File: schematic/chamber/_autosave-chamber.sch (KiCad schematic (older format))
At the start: 13 parts

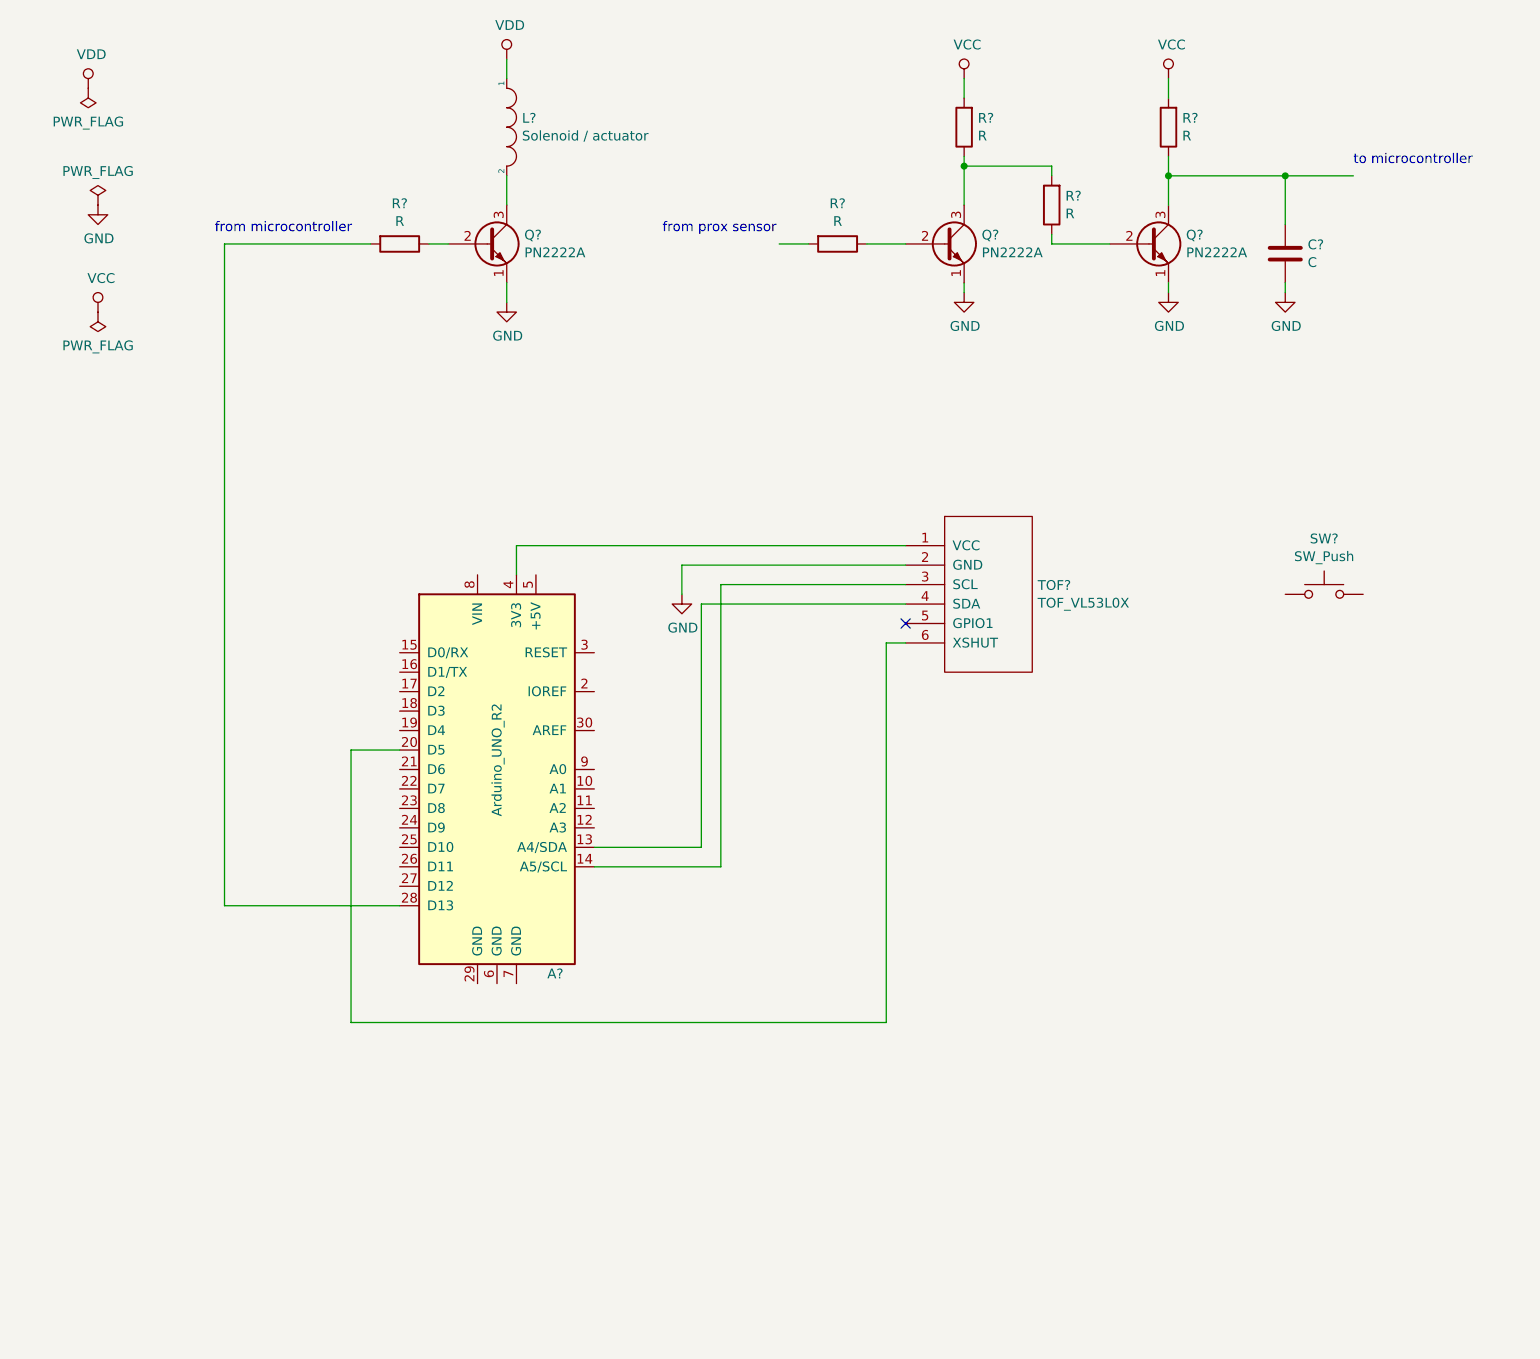
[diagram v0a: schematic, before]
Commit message: remove unused declarations
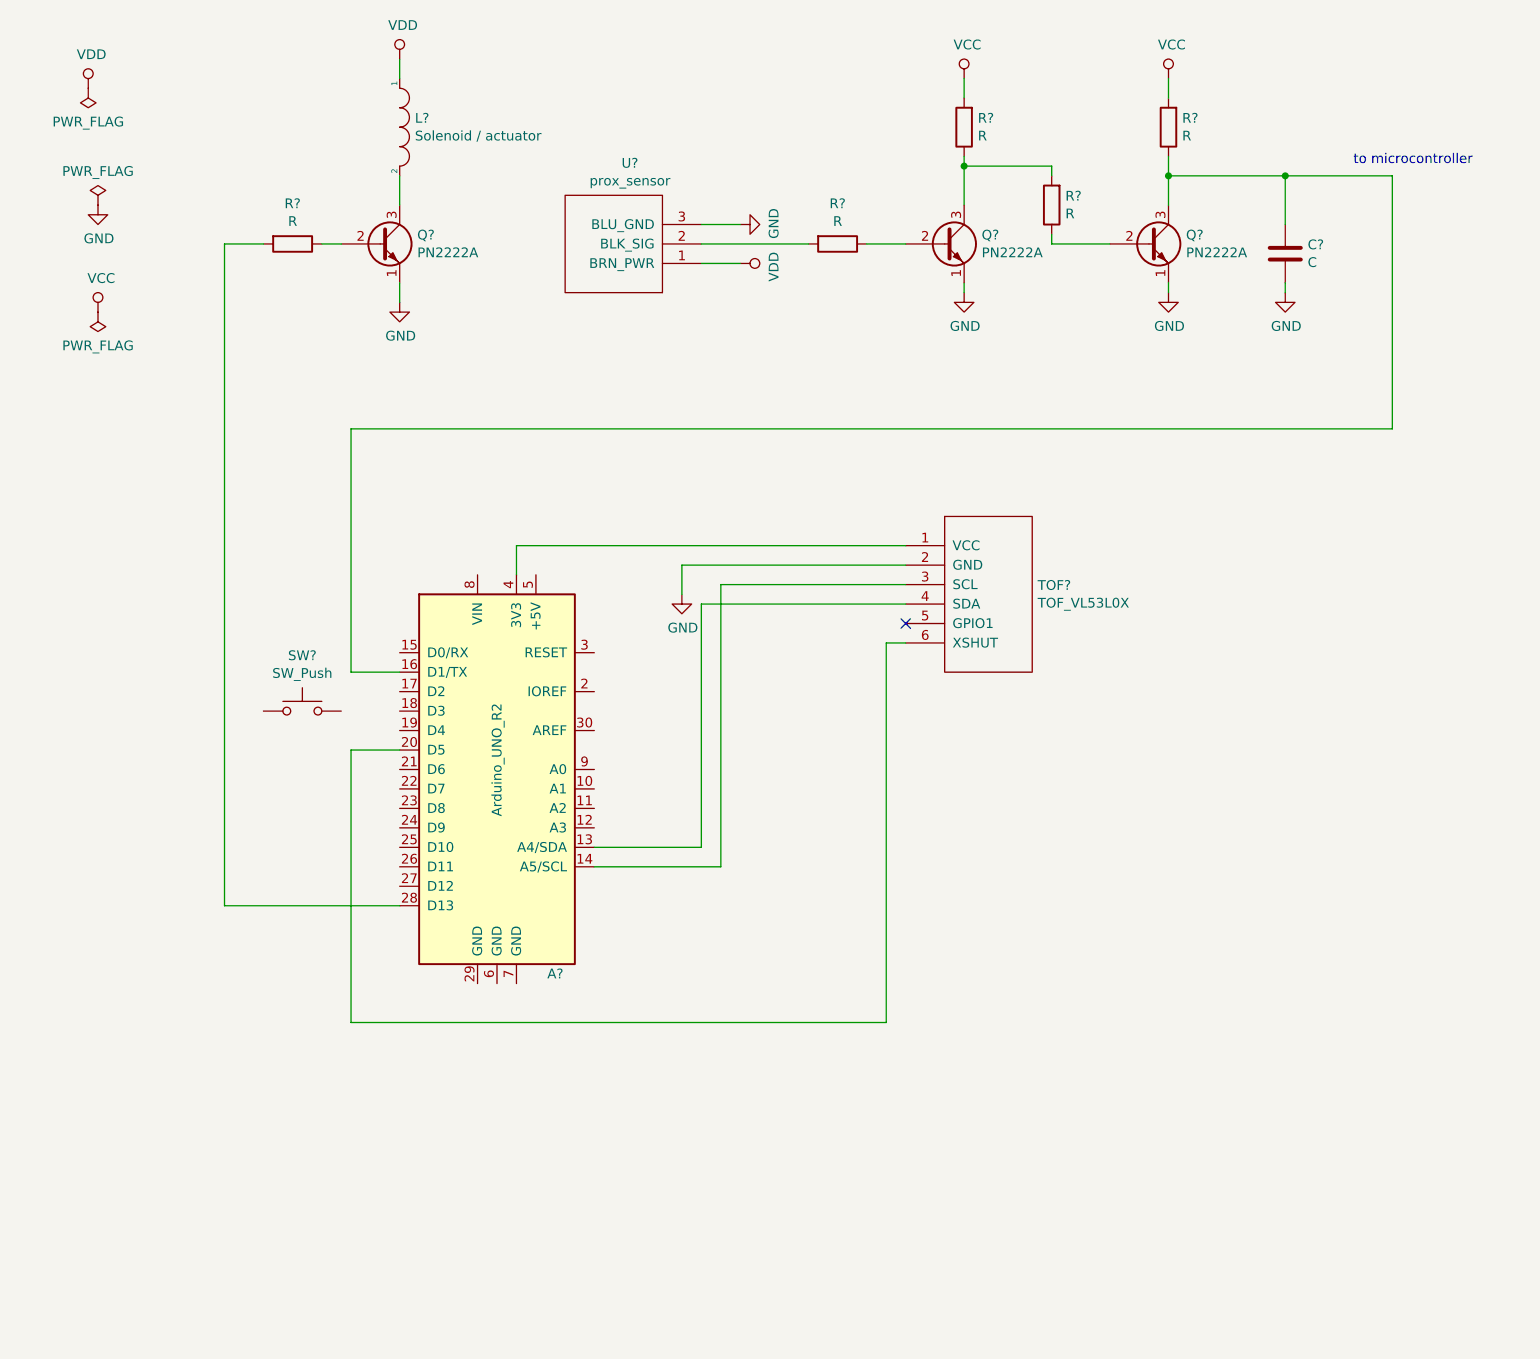
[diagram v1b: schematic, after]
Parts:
- added U?: prox_sensor, symbol custom:prox_sensor
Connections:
- wire segments 40 -> 46
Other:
- note removed: "from microcontroller"
- note removed: "from prox sensor"
- moved on the sheet: L?, Q?, R?, SW?
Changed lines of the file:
@@
 L Transistor_BJT:PN2222A Q?
 U 1 1 5DD49809
-P 3200 1750
-F 0 "Q?" H 3390 1796 50  0000 L CNN
-F 1 "PN2222A" H 3390 1705 50  0000 L CNN
-F 2 "Package_TO_SOT_THT:TO-92_Inline" H 3400 1675 50  0001 L CIN
-F 3 "http://www.fairchildsemi.com/ds/PN/PN2222A.pdf" H 3200 1750 50  0001 L CNN
-	1    3200 1750
+P 2650 1750
+F 0 "Q?" H 2840 1796 50  0000 L CNN
+F 1 "PN2222A" H 2840 1705 50  0000 L CNN
+F 2 "Package_TO_SOT_THT:TO-92_Inline" H 2850 1675 50  0001 L CIN
+F 3 "http://www.fairchildsemi.com/ds/PN/PN2222A.pdf" H 2650 1750 50  0001 L CNN
+	1    2650 1750
 	1    0    0    -1
 $EndComp
@@
 L Device:R R?
 U 1 1 5DD4B315
-P 2750 1750
-F 0 "R?" V 2543 1750 50  0000 C CNN
-F 1 "R" V 2634 1750 50  0000 C CNN
-F 2 "" V 2680 1750 50  0001 C CNN
-F 3 "~" H 2750 1750 50  0001 C CNN
-	1    2750 1750
+P 2200 1750
+F 0 "R?" V 1993 1750 50  0000 C CNN
+F 1 "R" V 2084 1750 50  0000 C CNN
+F 2 "" V 2130 1750 50  0001 C CNN
+F 3 "~" H 2200 1750 50  0001 C CNN
+	1    2200 1750
 	0    1    1    0
 $EndComp
@@
 $EndComp
 Wire Wire Line
-	3000 1750 2900 1750
+	2450 1750 2350 1750
 $Comp
 L power:VCC #PWR?
@@
 Wire Wire Line
 	6700 1400 7300 1400
-Wire Wire Line
-	7300 1400 7650 1400
 Connection ~ 7300 1400
 $Comp
@@
 L pspice:INDUCTOR L?
 U 1 1 5DD632F6
-P 3300 1150
-F 0 "L?" V 3254 1228 50  0000 L CNN
-F 1 "Solenoid / actuator" V 3345 1228 50  0000 L CNN
-F 2 "" H 3300 1150 50  0001 C CNN
-F 3 "~" H 3300 1150 50  0001 C CNN
-	1    3300 1150
+P 2750 1150
+F 0 "L?" V 2704 1228 50  0000 L CNN
+F 1 "Solenoid / actuator" V 2795 1228 50  0000 L CNN
+F 2 "" H 2750 1150 50  0001 C CNN
+F 3 "~" H 2750 1150 50  0001 C CNN
+	1    2750 1150
 	0    1    1    0
 $EndComp
 Wire Wire Line
-	3300 1400 3300 1550
+	2750 1400 2750 1550
 $Comp
 L power:GND #PWR?
 U 1 1 5DD64D74
-P 3300 2050
-F 0 "#PWR?" H 3300 1800 50  0001 C CNN
-F 1 "GND" H 3305 1877 50  0000 C CNN
-F 2 "" H 3300 2050 50  0001 C CNN
-F 3 "" H 3300 2050 50  0001 C CNN
-	1    3300 2050
-	1    0    0    -1
-$EndComp
-Wire Wire Line
-	3300 2050 3300 1950
+P 2750 2050
+F 0 "#PWR?" H 2750 1800 50  0001 C CNN
+F 1 "GND" H 2755 1877 50  0000 C CNN
+F 2 "" H 2750 2050 50  0001 C CNN
+F 3 "" H 2750 2050 50  0001 C CNN
+	1    2750 2050
+	1    0    0    -1
+$EndComp
+Wire Wire Line
+	2750 2050 2750 1950
 $Comp
 L power:PWR_FLAG #FLG?
@@
 L power:VDD #PWR?
 U 1 1 5DD6E1D7
-P 3300 800
-F 0 "#PWR?" H 3300 650 50  0001 C CNN
-F 1 "VDD" H 3317 973 50  0000 C CNN
-F 2 "" H 3300 800 50  0001 C CNN
-F 3 "" H 3300 800 50  0001 C CNN
-	1    3300 800
-	1    0    0    -1
-$EndComp
-Wire Wire Line
-	3300 800  3300 900
+P 2750 800
+F 0 "#PWR?" H 2750 650 50  0001 C CNN
+F 1 "VDD" H 2767 973 50  0000 C CNN
+F 2 "" H 2750 800 50  0001 C CNN
+F 3 "" H 2750 800 50  0001 C CNN
+	1    2750 800
+	1    0    0    -1
+$EndComp
+Wire Wire Line
+	2750 800  2750 900
 Wire Wire Line
 	5150 1750 5350 1750
-Wire Wire Line
-	4850 1750 4700 1750
-Text Notes 4100 1700 0    50   ~ 0
-from prox sensor
 Text Notes 7650 1350 0    50   ~ 0
 to microcontroller
-Text Notes 1800 1700 0    50   ~ 0
-from microcontroller
 $Comp
 L custom:TOF_VL53L0X TOF?
@@
 L Switch:SW_Push SW?
 U 1 1 5DDF2A14
-P 7500 3550
-F 0 "SW?" H 7500 3835 50  0000 C CNN
-F 1 "SW_Push" H 7500 3744 50  0000 C CNN
-F 2 "" H 7500 3750 50  0001 C CNN
-F 3 "~" H 7500 3750 50  0001 C CNN
-	1    7500 3550
+P 2250 4150
+F 0 "SW?" H 2250 4435 50  0000 C CNN
+F 1 "SW_Push" H 2250 4344 50  0000 C CNN
+F 2 "" H 2250 4350 50  0001 C CNN
+F 3 "~" H 2250 4350 50  0001 C CNN
+	1    2250 4150
 	1    0    0    -1
 $EndComp
@@
 	1850 5150 1850 1750
 Wire Wire Line
-	1850 1750 2600 1750
+	7850 1400 7850 2700
+Wire Wire Line
+	7850 2700 2500 2700
+Wire Wire Line
+	2500 2700 2500 3950
+Wire Wire Line
+	2500 3950 2750 3950
+Wire Wire Line
+	7300 1400 7850 1400
+$Comp
+L custom:prox_sensor U?
+U 1 1 5DE038E4
+P 3900 1750
+F 0 "U?" H 3867 1335 50  0000 C CNN
+F 1 "prox_sensor" H 3867 1426 50  0000 C CNN
+F 2 "" H 3650 1750 50  0001 C CNN
+F 3 "" H 3650 1750 50  0001 C CNN
+	1    3900 1750
+	-1   0    0    1
+$EndComp
+Wire Wire Line
+	1850 1750 2050 1750
+Wire Wire Line
+	4300 1750 4850 1750
+$Comp
+L power:VDD #PWR?
+U 1 1 5DE0E666
+P 4500 1850
+F 0 "#PWR?" H 4500 1700 50  0001 C CNN
+F 1 "VDD" H 4517 2023 50  0000 C CNN
+F 2 "" H 4500 1850 50  0001 C CNN
+F 3 "" H 4500 1850 50  0001 C CNN
+	1    4500 1850
+	0    1    1    0
+$EndComp
+Wire Wire Line
+	4500 1850 4300 1850
+$Comp
+L power:GND #PWR?
+U 1 1 5DE10F35
+P 4500 1650
+F 0 "#PWR?" H 4500 1400 50  0001 C CNN
+F 1 "GND" H 4505 1477 50  0000 C CNN
+F 2 "" H 4500 1650 50  0001 C CNN
+F 3 "" H 4500 1650 50  0001 C CNN
+	1    4500 1650
+	0    -1   -1   0
+$EndComp
+Wire Wire Line
+	4500 1650 4300 1650
 $EndSCHEMATC

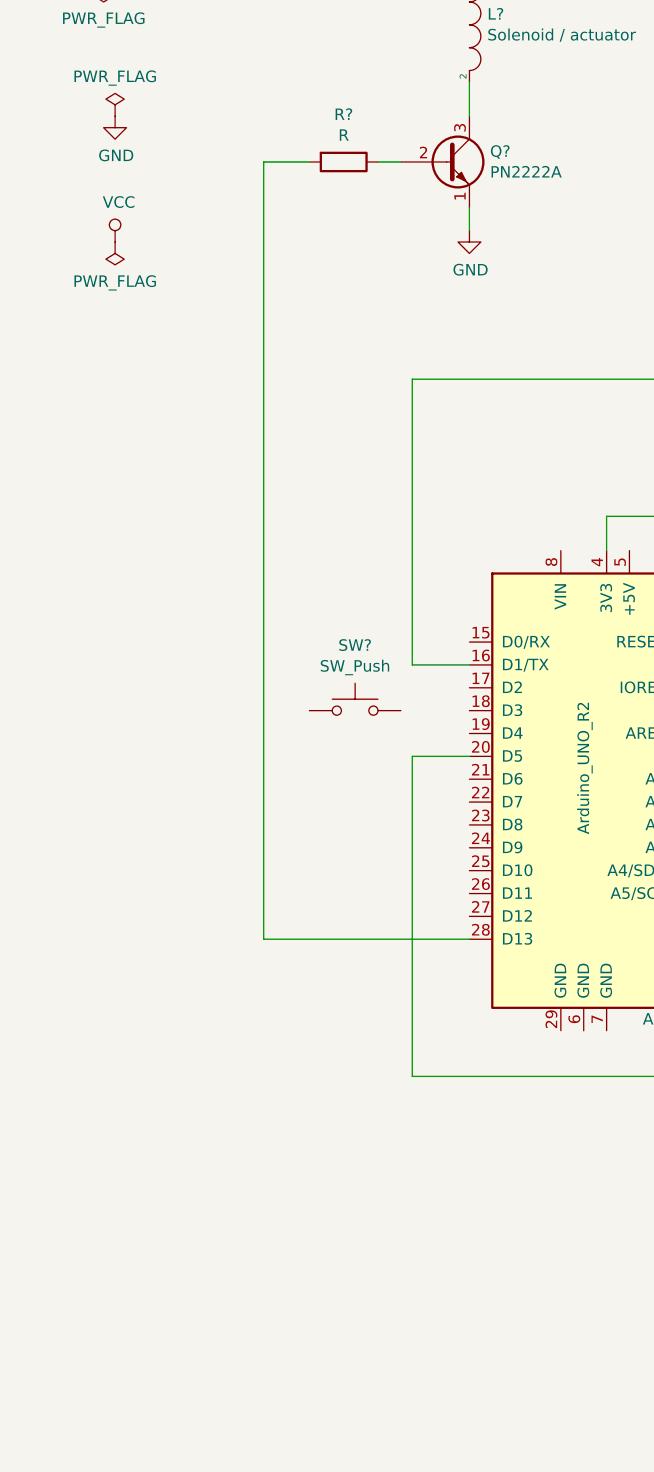
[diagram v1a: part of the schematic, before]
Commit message: change solenoid pin to 10 add wireless sensor to the schematic
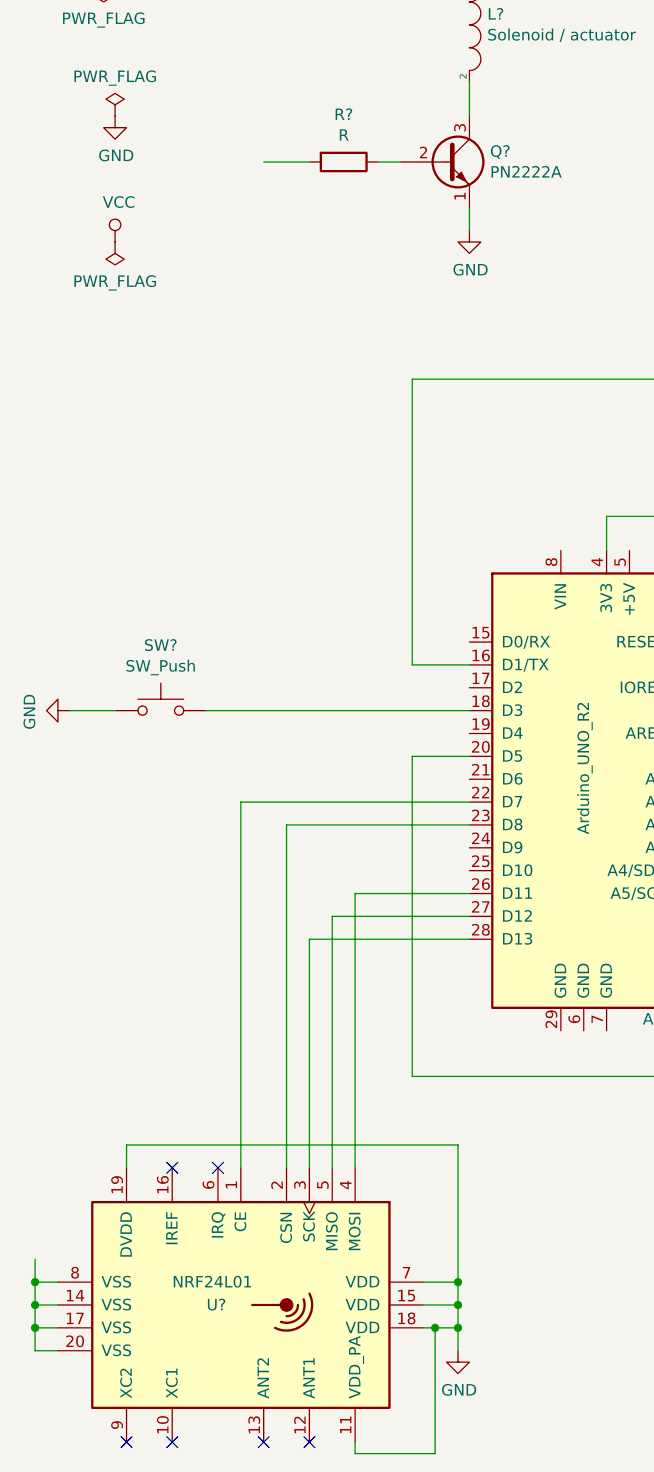
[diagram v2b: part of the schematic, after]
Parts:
- added U?: NRF24L01, Package_DFN_QFN:QFN-20-1EP_4x4mm_P0.5mm_EP2.5x2.5mm, symbol RF:NRF24L01
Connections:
- net GND: now also SW?.1, U?.11 (VDD_PA), U?.15 (VDD), U?.18 (VDD), U?.19 (DVDD), U?.7 (VDD)
- net at R?.2: no longer A?.28 (D13)
- net at A?.18 (D3): now also SW?.2
- net at A?.22 (D7): now also U?.1 (CE)
- net at A?.23 (D8): now also U?.2 (CSN)
- net at A?.26 (D11): now also U?.4 (MOSI)
- net at A?.27 (D12): now also U?.5 (MISO)
- new net: A?.28 (D13), U?.3 (SCK)
- new net: U?.14 (VSS), U?.17 (VSS), U?.20 (VSS), U?.8 (VSS)
- no-connect marks 1 -> 7
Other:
- moved on the sheet: SW?
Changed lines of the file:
@@
 L Switch:SW_Push SW?
 U 1 1 5DDF2A14
-P 2250 4150
-F 0 "SW?" H 2250 4435 50  0000 C CNN
-F 1 "SW_Push" H 2250 4344 50  0000 C CNN
-F 2 "" H 2250 4350 50  0001 C CNN
-F 3 "~" H 2250 4350 50  0001 C CNN
-	1    2250 4150
+P 1400 4150
+F 0 "SW?" H 1400 4435 50  0000 C CNN
+F 1 "SW_Push" H 1400 4344 50  0000 C CNN
+F 2 "" H 1400 4350 50  0001 C CNN
+F 3 "~" H 1400 4350 50  0001 C CNN
+	1    1400 4150
 	1    0    0    -1
 $EndComp
@@
 Wire Wire Line
 	5250 3800 5350 3800
-Wire Wire Line
-	2750 5150 1850 5150
-Wire Wire Line
-	1850 5150 1850 1750
 Wire Wire Line
 	7850 1400 7850 2700
@@
 Wire Wire Line
 	4500 1650 4300 1650
+Wire Wire Line
+	1600 4150 2750 4150
+$Comp
+L power:GND #PWR?
+U 1 1 5DE16672
+P 1000 4150
+F 0 "#PWR?" H 1000 3900 50  0001 C CNN
+F 1 "GND" H 1005 3977 50  0000 C CNN
+F 2 "" H 1000 4150 50  0001 C CNN
+F 3 "" H 1000 4150 50  0001 C CNN
+	1    1000 4150
+	0    1    1    0
+$EndComp
+Wire Wire Line
+	1200 4150 1000 4150
+$Comp
+L RF:NRF24L01 U?
+U 1 1 5DE18900
+P 1750 6750
+F 0 "U?" V 1750 6600 50  0000 L CNN
+F 1 "NRF24L01" V 1650 6450 50  0000 L CNN
+F 2 "Package_DFN_QFN:QFN-20-1EP_4x4mm_P0.5mm_EP2.5x2.5mm" H 1950 7550 50  0001 L CIN
+F 3 "http://www.nordicsemi.com/eng/content/download/2730/34105/file/nRF24L01_Product_Specification_v2_0.pdf" H 1750 6850 50  0001 C CNN
+	1    1750 6750
+	0    1    1    0
+$EndComp
+Wire Wire Line
+	1950 6150 1950 4650
+Wire Wire Line
+	1950 4650 2750 4650
+Wire Wire Line
+	2250 6150 2250 4950
+Wire Wire Line
+	2250 4950 2750 4950
+Wire Wire Line
+	1750 6150 1750 4550
+Wire Wire Line
+	1750 4550 2750 4550
+Wire Wire Line
+	2050 6150 2050 5150
+Wire Wire Line
+	2050 5150 2750 5150
+Wire Wire Line
+	2150 6150 2150 5050
+Wire Wire Line
+	2150 5050 2750 5050
+Wire Wire Line
+	2550 6650 2700 6650
+Wire Wire Line
+	2700 6650 2700 6750
+Wire Wire Line
+	2700 6850 2600 6850
+Wire Wire Line
+	2550 6750 2700 6750
+Connection ~ 2700 6750
+Wire Wire Line
+	2700 6750 2700 6850
+Wire Wire Line
+	2700 6850 2700 6950
+Connection ~ 2700 6850
+$Comp
+L power:GND #PWR?
+U 1 1 5DE2B4F4
+P 2700 6950
+F 0 "#PWR?" H 2700 6700 50  0001 C CNN
+F 1 "GND" H 2705 6777 50  0000 C CNN
+F 2 "" H 2700 6950 50  0001 C CNN
+F 3 "" H 2700 6950 50  0001 C CNN
+	1    2700 6950
+	1    0    0    -1
+$EndComp
+Wire Wire Line
+	1250 6150 1250 6050
+Wire Wire Line
+	1250 6050 2700 6050
+Wire Wire Line
+	2700 6050 2700 6650
+Connection ~ 2700 6650
+Wire Wire Line
+	950  6650 850  6650
+Wire Wire Line
+	850  6650 850  6750
+Wire Wire Line
+	850  6950 950  6950
+Wire Wire Line
+	950  6850 850  6850
+Connection ~ 850  6850
+Wire Wire Line
+	850  6850 850  6950
+Wire Wire Line
+	850  6750 950  6750
+Connection ~ 850  6750
+Wire Wire Line
+	850  6750 850  6850
+Wire Wire Line
+	2250 7350 2250 7400
+Wire Wire Line
+	2250 7400 2600 7400
+Wire Wire Line
+	2600 7400 2600 6850
+Connection ~ 2600 6850
+Wire Wire Line
+	2600 6850 2550 6850
+NoConn ~ 1450 6150
+NoConn ~ 1650 6150
+NoConn ~ 1250 7350
+NoConn ~ 1450 7350
+NoConn ~ 1850 7350
+NoConn ~ 2050 7350
+Wire Wire Line
+	850  6550 850  6650
+Connection ~ 850  6650
 $EndSCHEMATC
